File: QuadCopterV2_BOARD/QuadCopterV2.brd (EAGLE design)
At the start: 108.1 x 108.1 mm, 29 parts, among them IC1 EK-TM4C123GXLP, U1 GY-63MS5611, U10 ESC-30AMS5611, U2 GY-521MPU6050, U3 GY-63MS5611, U4 MCP1825S-3302E/DBP1, U5 MCP1825S-3302E/DBP1, U6 MCP1825S-3302E/DBP1, U7 ESC-30AMS5611, U8 ESC-30AMS5611, U9 ESC-30AMS5611

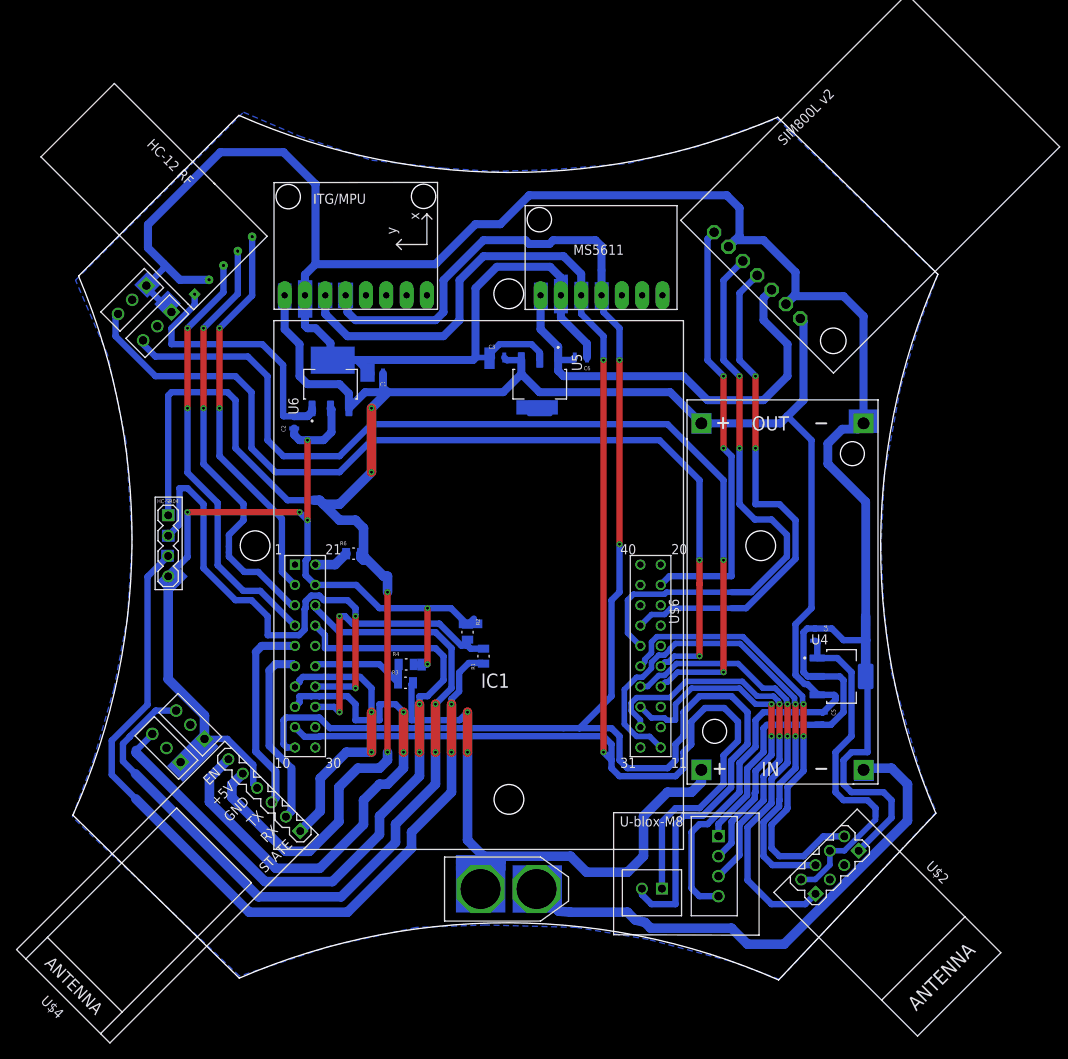
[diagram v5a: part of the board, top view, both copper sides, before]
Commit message: added board rendered version
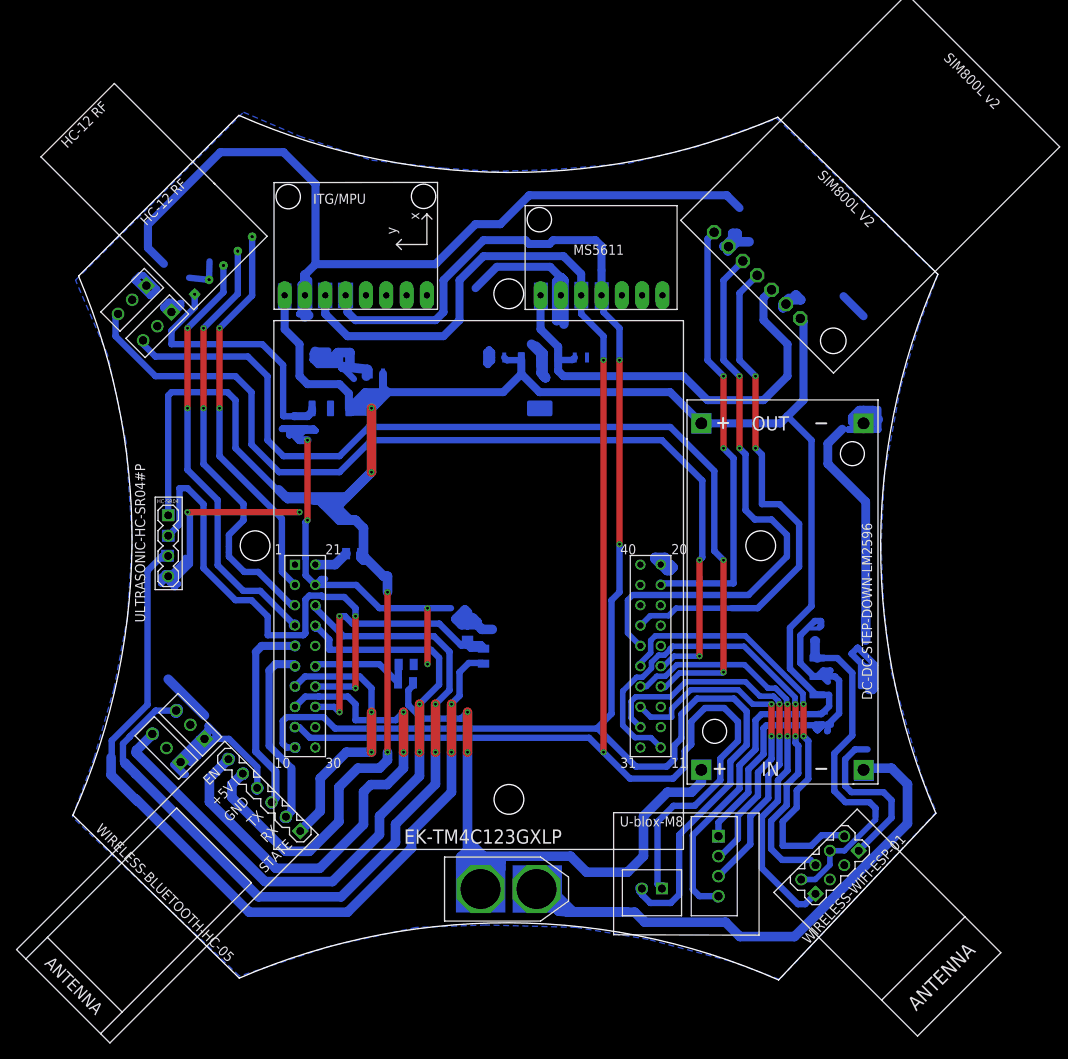
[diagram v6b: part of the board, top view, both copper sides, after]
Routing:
- net GND: track 476.2 -> 549.6 mm
- net N$36: track 0.00 -> 13.3 mm
- net N$50: track 0.00 -> 10.4 mm
- net N$122: track 0.00 -> 9.20 mm
- net N$103: track 0.00 -> 6.87 mm
- net N$49: track 0.00 -> 6.77 mm
- net N$37: track 0.00 -> 5.65 mm
- net I2C_SDA_1: track 214.0 -> 208.9 mm
- net VBAT+: track 72.5 -> 76.2 mm
- net U3_TX: track 56.3 -> 52.8 mm
- net N$39: track 0.00 -> 3.43 mm
- net N$9: track 0.00 -> 3.12 mm
- net I2C_SCL_1: track 199.2 -> 196.4 mm
- net U3_RX: track 57.1 -> 55.1 mm
- net N$104: track 0.00 -> 1.89 mm
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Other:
- board text added: "HC-12 RF"
- board text added: "SIM800L V2"

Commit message: board sended to production
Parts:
- moved C4 2.00 mm to (92.4, 24.5)
- moved U4 2.00 mm to (95.7, 19.5)
- moved C5 1.00 mm to (94.4, 12.0)
- moved U$7 0.29 mm to (46.1, -8.82)
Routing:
- net PB7: track 119.5 -> 205.5 mm, vias 2 -> 1
- net PB6: track 120.6 -> 204.6 mm, vias 2 -> 1
- net VBAT-: track 66.7 -> 133.8 mm
- net PA5: track 65.5 -> 11.0 mm, vias 2 -> 0
- net VBAT+: track 76.2 -> 114.8 mm, vias 2 -> 0
- net PA2: track 64.1 -> 29.2 mm, vias 2 -> 0
- net U3_RX: track 55.1 -> 88.1 mm, vias 2 -> 0
- net PB2: track 54.8 -> 74.4 mm, vias 2 -> 0
- net PE1: track 62.5 -> 43.0 mm, vias 2 -> 0
- net I2C_SCL_1: track 196.4 -> 214.4 mm, vias 2 -> 4
- net U2_TX: track 49.2 -> 33.2 mm, vias 2 -> 0
- net N$36: track 13.3 -> 0.00 mm
- net N$50: track 10.4 -> 0.00 mm
- net U2_RX: track 41.6 -> 32.2 mm, vias 2 -> 0
- net N$122: track 9.20 -> 0.00 mm
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- added copper zone on layer 1, net 5V0
